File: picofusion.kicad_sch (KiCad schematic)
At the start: 39 parts, among them J1 NORTH, J2 EAST, J3 WEST, J4 SOUTH, U1 W25Q16, U2 RP2040, U3 TLV71333PDQNT, U7 MCP2544FD, Y1 12MHz

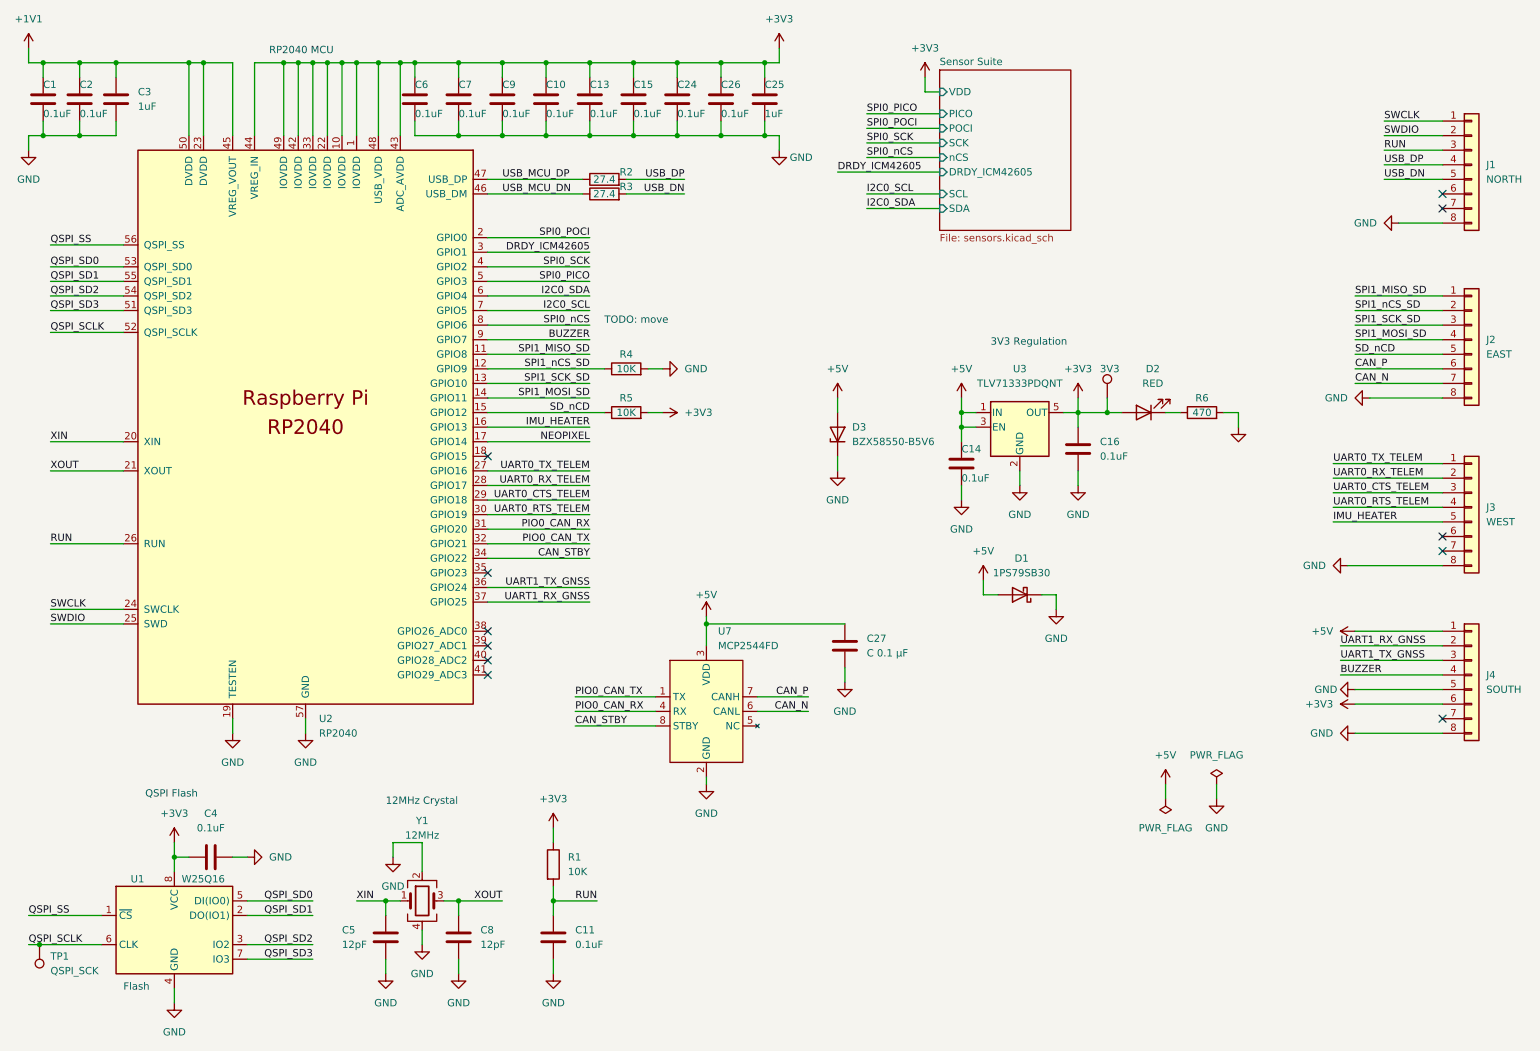
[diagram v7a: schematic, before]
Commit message: layout: update castellations, pinout, reorder
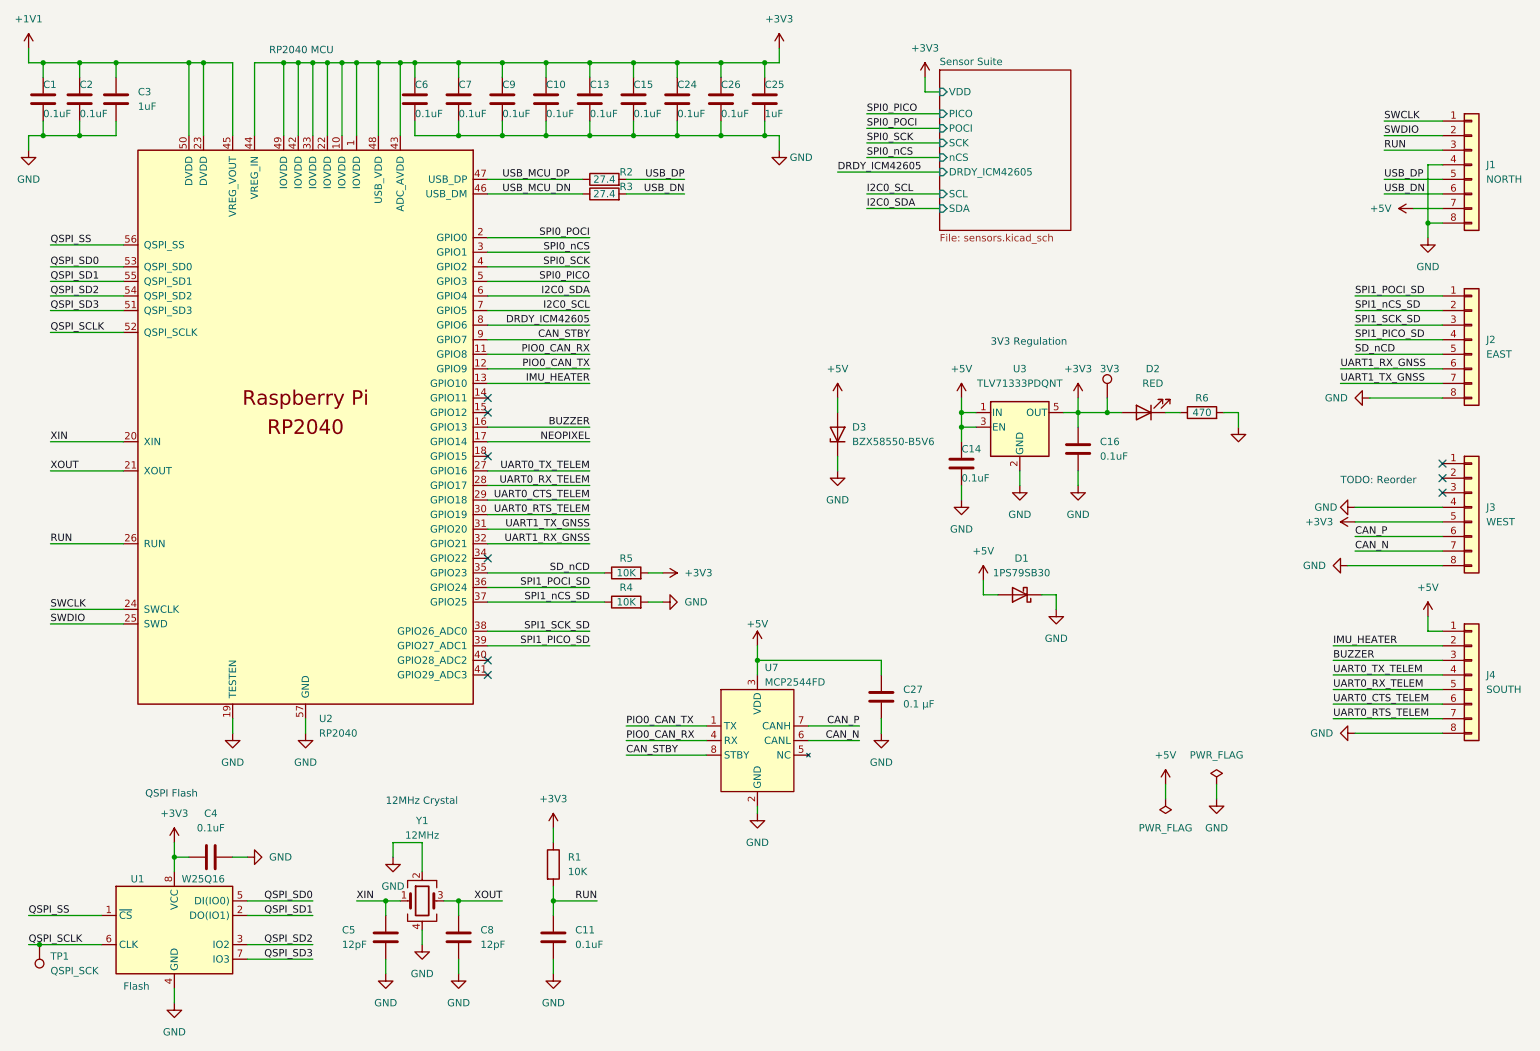
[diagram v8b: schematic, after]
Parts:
- C27: value C 0.1 µF -> 0.1 µF
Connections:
- net +3V3: now also J3.5 (Pin_5); no longer J4.6 (Pin_6)
- net +5V: now also J1.7 (Pin_7)
- net BUZZER: now also J4.3 (Pin_3), U2.16 (GPIO13); no longer J4.4 (Pin_4), U2.9 (GPIO7)
- net CAN_N: now also J3.7 (Pin_7); no longer J2.7 (Pin_7)
- net CAN_P: now also J3.6 (Pin_6); no longer J2.6 (Pin_6)
- net CAN_STBY: now also U2.9 (GPIO7); no longer U2.34 (GPIO22)
- net DRDY_ICM42605: now also U2.8 (GPIO6); no longer U2.3 (GPIO1)
- net GND: now also J1.4 (Pin_4), J3.4 (Pin_4); no longer J4.5 (Pin_5)
- net IMU_HEATER: now also J4.2 (Pin_2), U2.13 (GPIO10); no longer J3.5 (Pin_5), U2.16 (GPIO13)
- net PIO0_CAN_RX: now also U2.11 (GPIO8); no longer U2.31 (GPIO20)
- net PIO0_CAN_TX: now also U2.12 (GPIO9); no longer U2.32 (GPIO21)
- net SD_nCD: now also U2.35 (GPIO23); no longer U2.15 (GPIO12)
- net SPI0_nCS: now also U2.3 (GPIO1); no longer U2.8 (GPIO6)
- net SPI1_SCK_SD: now also U2.38 (GPIO26_ADC0); no longer U2.13 (GPIO10)
- net SPI1_nCS_SD: now also U2.37 (GPIO25); no longer U2.12 (GPIO9)
- net UART0_CTS_TELEM: now also J4.6 (Pin_6); no longer J3.3 (Pin_3)
- net UART0_RTS_TELEM: now also J4.7 (Pin_7); no longer J3.4 (Pin_4)
- net UART0_RX_TELEM: now also J4.5 (Pin_5); no longer J3.2 (Pin_2)
- net UART0_TX_TELEM: now also J4.4 (Pin_4); no longer J3.1 (Pin_1)
- net UART1_RX_GNSS: now also J2.6 (Pin_6), U2.32 (GPIO21); no longer J4.2 (Pin_2), U2.37 (GPIO25)
- net UART1_TX_GNSS: now also J2.7 (Pin_7), U2.31 (GPIO20); no longer J4.3 (Pin_3), U2.36 (GPIO24)
- net USB_DN: now also J1.6 (Pin_6); no longer J1.5 (Pin_5)
- net USB_DP: now also J1.5 (Pin_5); no longer J1.4 (Pin_4)
- net SPI1_PICO_SD: now reaches U2.39 (GPIO27_ADC1)
- net SPI1_PICO_SD: now also J2.4 (Pin_4)
- net SPI1_MISO_SD renamed SPI1_POCI_SD
- net SPI1_POCI_SD: now also U2.36 (GPIO24); no longer U2.11 (GPIO8)
- net SPI1_MOSI_SD: no longer names the net of U2.14 (GPIO11)
- net SPI1_MOSI_SD: no longer J2.4 (Pin_4)
- no-connect marks 11 -> 9
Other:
- note added: "TODO: Reorder"
- note removed: "TODO: move"
- moved on the sheet: C27, R4, R5, U7
